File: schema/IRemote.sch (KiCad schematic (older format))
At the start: 1 part

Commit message: led driver MOS, correct opamp
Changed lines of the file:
@@
 F3 "DECODER_INPUT" I L 4800 4800 60
 $EndSheet
-Wire Bus Line
-	2400 1350 8850 1350
-Wire Bus Line
-	8850 1350 8850 3450
-Wire Bus Line
-	8850 3450 2400 3450
-Wire Bus Line
-	2400 3450 2400 1350
-Wire Bus Line
-	2400 3750 8900 3750
-Wire Bus Line
-	8900 3750 8900 6050
-Wire Bus Line
-	8900 6050 2400 6050
-Wire Bus Line
-	2400 6050 2400 3750
 Text Notes 2500 4000 0    100  ~ 0
 IR_RECEIVER
 Text Notes 2500 1600 0    100  ~ 0
 IR_REMOTE
+Wire Notes Line
+	2400 3750 8900 3750
+Wire Notes Line
+	8900 3750 8900 6050
+Wire Notes Line
+	8900 6050 2400 6050
+Wire Notes Line
+	2400 6050 2400 3750
+Wire Notes Line
+	2400 3450 8850 3450
+Wire Notes Line
+	8850 3450 8850 1350
+Wire Notes Line
+	8850 1350 2400 1350
+Wire Notes Line
+	2400 1350 2400 3450
 $EndSCHEMATC

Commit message: filter and comparator
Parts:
- gave numbers to parts that had none: 1
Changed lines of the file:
@@
 LIBS:contrib
 LIBS:valves
+LIBS:custom
 LIBS:IRemote-cache
 EELAYER 25 0
@@
 $EndSheet
 $Comp
-L GND #PWR?
+L GND #PWR2
 U 1 1 59103F43
 P 7500 2750
-F 0 "#PWR?" H 7500 2500 50  0001 C CNN
+F 0 "#PWR2" H 7500 2500 50  0001 C CNN
 F 1 "GND" H 7500 2600 50  0000 C CNN
 F 2 "" H 7500 2750 50  0000 C CNN
@@
 $EndComp
 $Comp
-L +BATT #PWR?
+L +BATT #PWR1
 U 1 1 59103F75
 P 7500 2350
-F 0 "#PWR?" H 7500 2200 50  0001 C CNN
+F 0 "#PWR1" H 7500 2200 50  0001 C CNN
 F 1 "+BATT" H 7500 2490 50  0000 C CNN
 F 2 "" H 7500 2350 50  0000 C CNN
@@
 $EndSheet
 $Comp
-L Battery-RESCUE-IRemote BT?
+L Battery-RESCUE-IRemote BT1
 U 1 1 59104416
 P 7500 2550
-F 0 "BT?" H 7600 2650 50  0000 L CNN
+F 0 "BT1" H 7600 2650 50  0000 L CNN
 F 1 "2x AAA battery" H 7600 2550 50  0000 L CNN
 F 2 "" V 7500 2610 50  0000 C CNN

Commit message: ouput driver
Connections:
- no-connect marks 0 -> 1
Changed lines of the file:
@@
 Wire Notes Line
 	2400 1350 2400 3450
+NoConn ~ 4100 2700
 $EndSCHEMATC

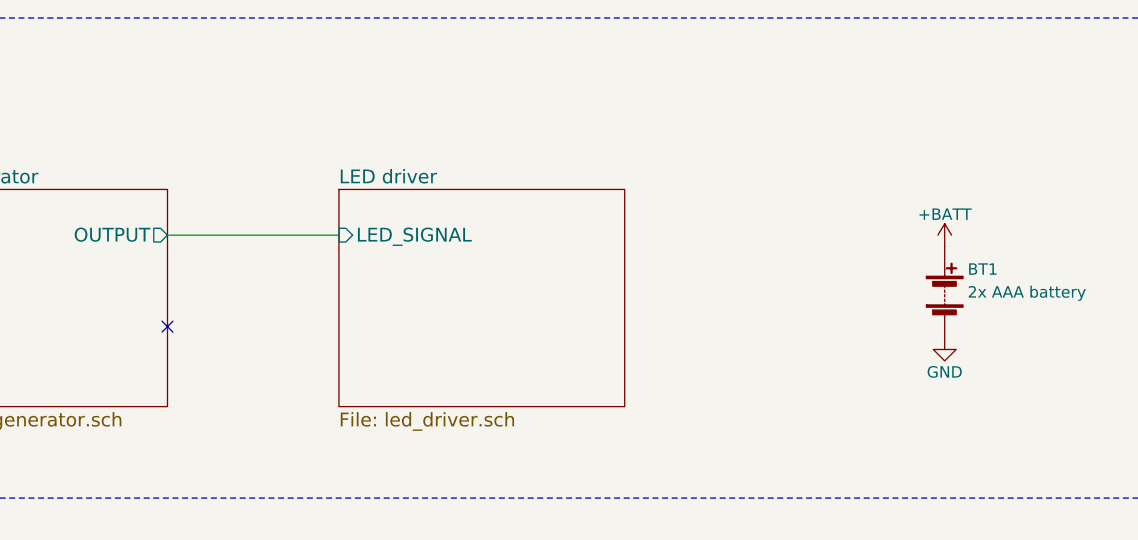
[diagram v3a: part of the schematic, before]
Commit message: reannotate schema
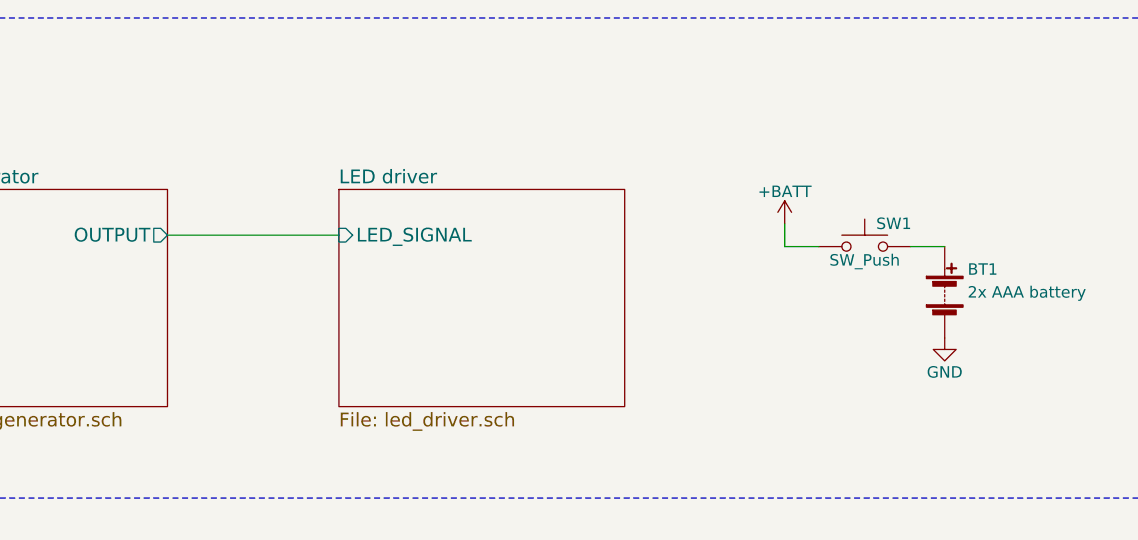
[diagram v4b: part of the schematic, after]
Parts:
- added SW1: SW_Push, symbol SW_Push
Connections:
- net +BATT: now also SW1.1; no longer BT1.1 (+)
- new net: BT1.1 (+), SW1.2
- no-connect marks 1 -> 0
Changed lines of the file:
@@
 Comment4 ""
 $EndDescr
-$Sheet
-S 2850 2100 1250 950
-U 5910364F
-F0 "Signal generator" 60
-F1 "signal_generator.sch" 60
-F2 "OUTPUT" O R 4100 2300 60
-$EndSheet
 $Comp
 L GND #PWR2
@@
 L +BATT #PWR1
 U 1 1 59103F75
-P 7500 2350
-F 0 "#PWR1" H 7500 2200 50  0001 C CNN
-F 1 "+BATT" H 7500 2490 50  0000 C CNN
-F 2 "" H 7500 2350 50  0000 C CNN
-F 3 "" H 7500 2350 50  0000 C CNN
-	1    7500 2350
+P 6800 2250
+F 0 "#PWR1" H 6800 2100 50  0001 C CNN
+F 1 "+BATT" H 6800 2390 50  0000 C CNN
+F 2 "" H 6800 2250 50  0000 C CNN
+F 3 "" H 6800 2250 50  0000 C CNN
+	1    6800 2250
 	1    0    0    -1
 $EndComp
@@
 Wire Notes Line
 	2400 1350 2400 3450
-NoConn ~ 4100 2700
+$Sheet
+S 2850 2100 1250 950
+U 5910364F
+F0 "Signal generator" 60
+F1 "signal_generator.sch" 60
+F2 "OUTPUT" O R 4100 2300 60
+$EndSheet
+$Comp
+L SW_Push SW1
+U 1 1 593A9694
+P 7150 2350
+F 0 "SW1" H 7200 2450 50  0000 L CNN
+F 1 "SW_Push" H 7150 2290 50  0000 C CNN
+F 2 "" H 7150 2550 50  0000 C CNN
+F 3 "" H 7150 2550 50  0000 C CNN
+	1    7150 2350
+	1    0    0    -1
+$EndComp
+Wire Wire Line
+	6800 2250 6800 2350
+Wire Wire Line
+	6800 2350 6950 2350
+Wire Wire Line
+	7350 2350 7500 2350
 $EndSCHEMATC

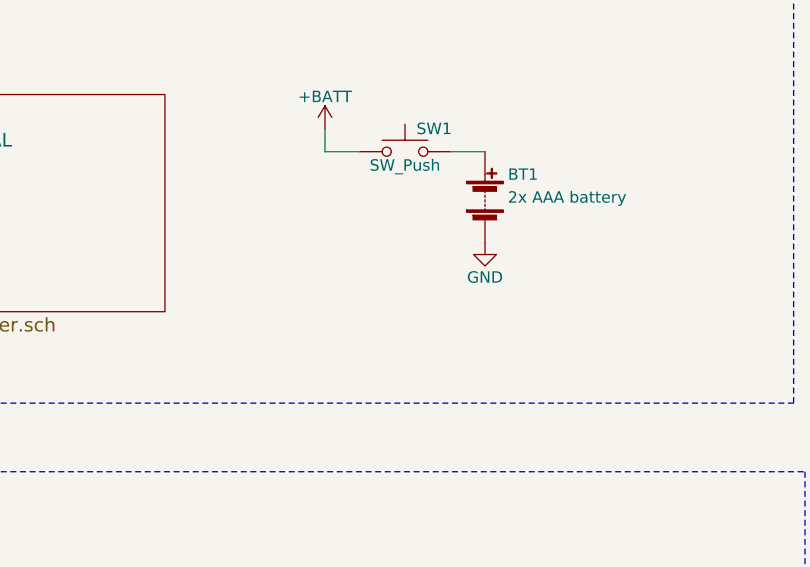
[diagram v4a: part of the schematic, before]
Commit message: Schematic done
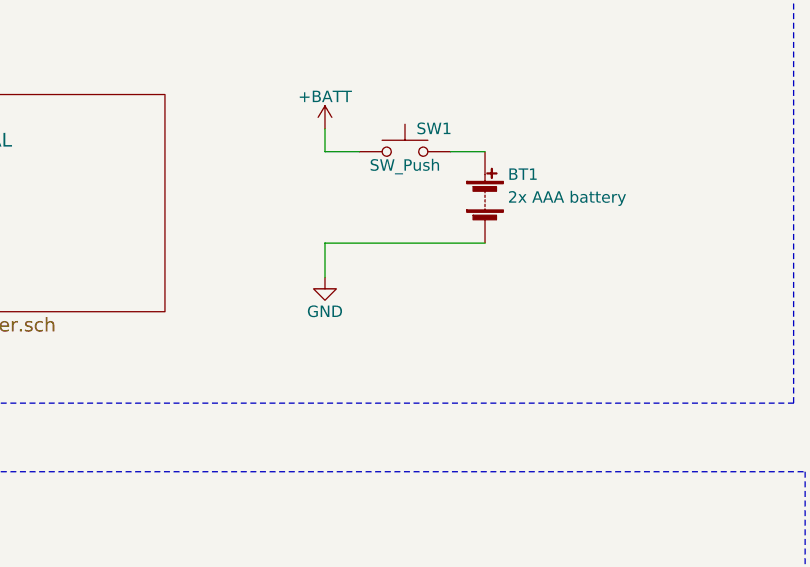
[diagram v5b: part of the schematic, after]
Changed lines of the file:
@@
 L GND #PWR2
 U 1 1 59103F43
-P 7500 2750
-F 0 "#PWR2" H 7500 2500 50  0001 C CNN
-F 1 "GND" H 7500 2600 50  0000 C CNN
-F 2 "" H 7500 2750 50  0000 C CNN
-F 3 "" H 7500 2750 50  0000 C CNN
-	1    7500 2750
+P 6800 2900
+F 0 "#PWR2" H 6800 2650 50  0001 C CNN
+F 1 "GND" H 6800 2750 50  0000 C CNN
+F 2 "" H 6800 2900 50  0000 C CNN
+F 3 "" H 6800 2900 50  0000 C CNN
+	1    6800 2900
 	1    0    0    -1
 $EndComp
@@
 Wire Wire Line
 	7350 2350 7500 2350
+Wire Wire Line
+	6800 2750 7500 2750
+Wire Wire Line
+	6800 2900 6800 2750
 $EndSCHEMATC
